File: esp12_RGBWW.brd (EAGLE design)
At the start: 51.1 x 34.9 mm, 35 parts, among them Q1 AOD2910SMD, Q2 AOD2910SMD, Q3 AOD2910SMD, Q4 AOD2910SMD, Q5 AOD2910SMD, U1 TPS5410DR

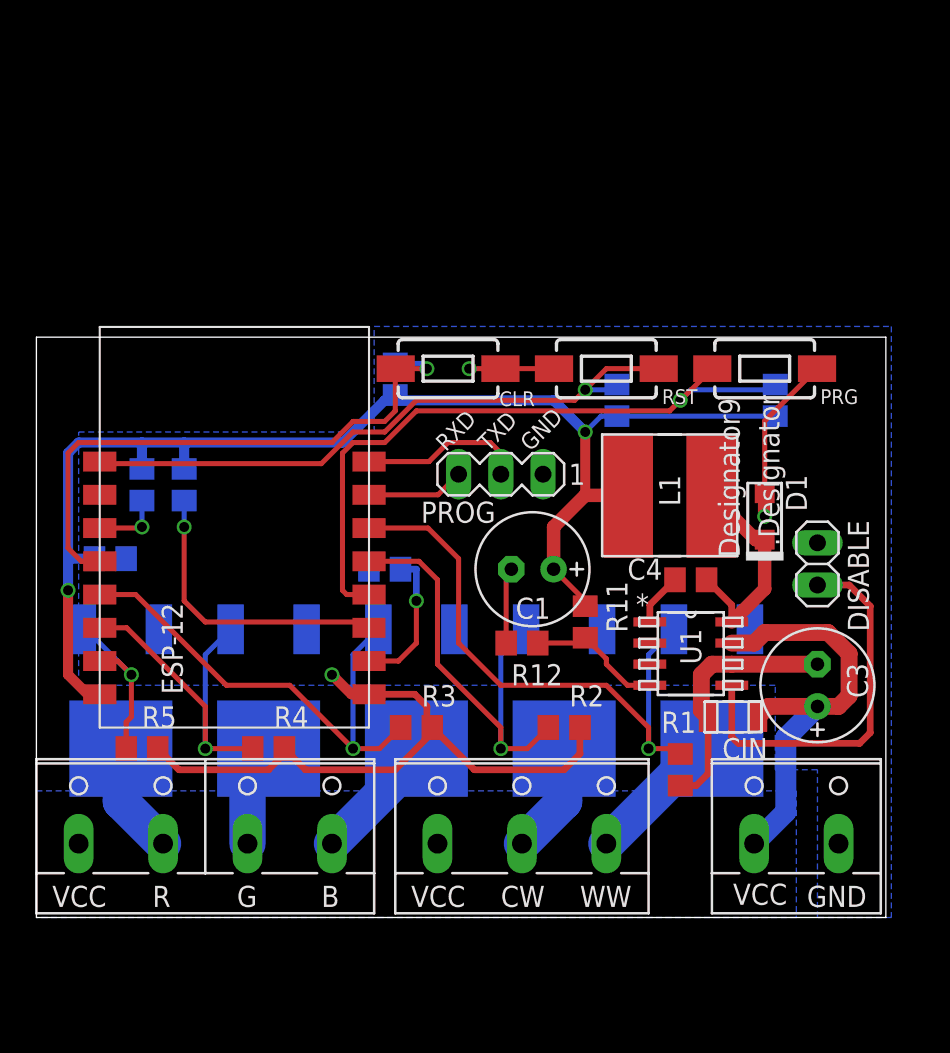
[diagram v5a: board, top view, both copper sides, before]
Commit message: some power supply improvements
added a snubber network to PH (140MHz) plus a 10nF cap on the +3V3 line
Added low impedance floodfills for +3V3 and PH where applicable
switched the location of the RST and PRG switches since it seems easier to have the RST on the outside
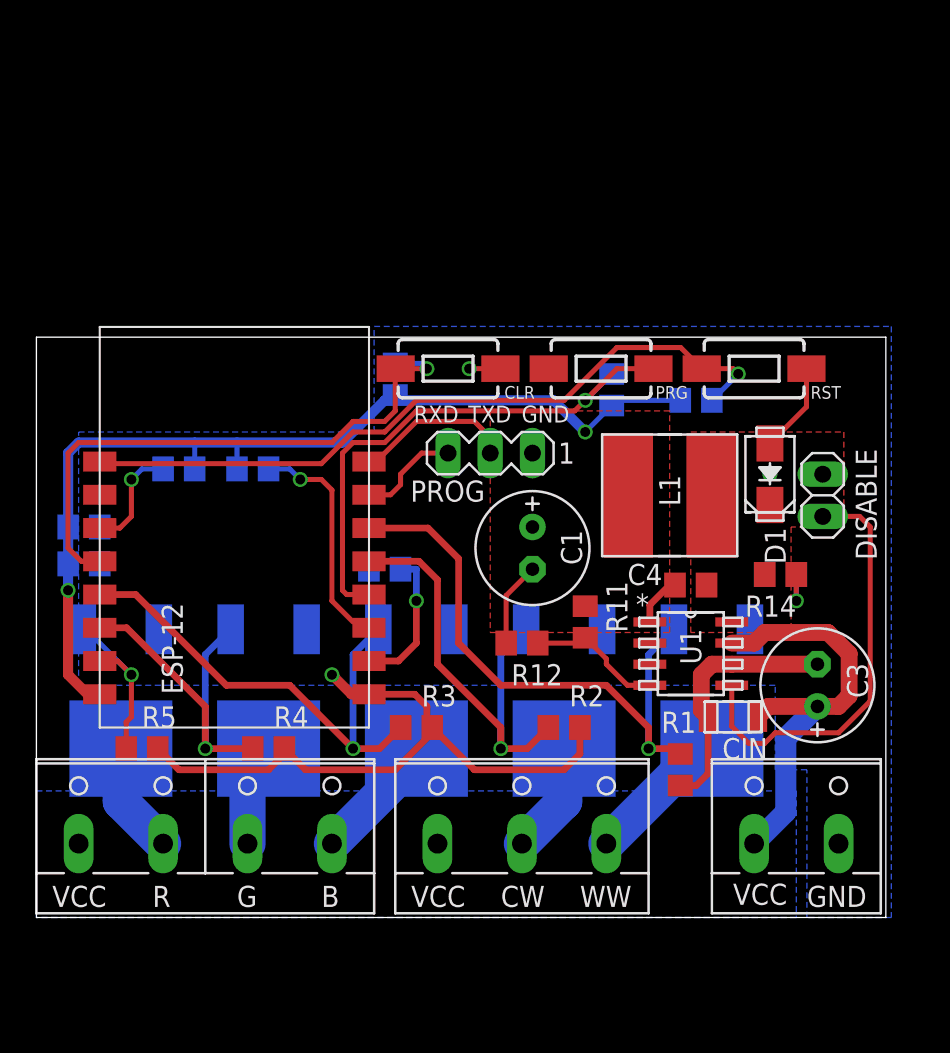
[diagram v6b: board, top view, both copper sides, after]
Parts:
- added C5: 10n, rcl:C0805
- added C6: 1.5p, rcl:C0805
- added R14: 1k, rcl:R0805
- D1: device AcceleratedDesigns_Lib:SOD-123F -> TI_Accelerated_Design_neu:SMA
- moved R13 9.86 mm to (33.3, 31.8)
- moved PRG 9.84 mm to (32.7, 33.0), turned to 180 degrees
- moved RST 8.89 mm to (41.9, 33.0), turned to 180 degrees
- moved R10 4.76 mm to (38.4, 31.1), turned to 180 degrees
- moved R7 4.24 mm to (11.7, 27.0), turned to 0 degrees
- moved DISABLE 4.14 mm to (46.0, 25.4), turned to 90 degrees
- moved D1 2.56 mm to (42.9, 26.7)
- moved C2 2.48 mm to (1.59, 23.5)
- moved R9 2.42 mm to (7.30, 27.0), turned to 180 degrees
- moved PROG 1.42 mm to (26.0, 27.9)
- moved C1 1.27 mm to (28.6, 22.2), turned to 270 degrees
- moved C4 0.32 mm to (38.1, 20.0)
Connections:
- new net SNUB: C6.1, R14.1
- net +3V3: now also C5.2
- net ENA: now also DISABLE.1; no longer DISABLE.2
- net GND: now also C5.1, C6.2, DISABLE.2; no longer DISABLE.1
- net PH: now also R14.2
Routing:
- net +3V3: track 83.9 -> 60.1 mm
- net PH: track 15.7 -> 3.40 mm
- net GND: track 76.0 -> 68.5 mm
- net PRG_S: track 40.4 -> 33.0 mm
- net RST_S: track 38.1 -> 44.3 mm
- net G2: track 17.8 -> 13.9 mm
- net SNUB: track 0.00 -> 3.18 mm, vias 0 -> 1
- net ENA: track 23.2 -> 25.9 mm
- net CH_PD: track 4.16 -> 6.59 mm
- added copper zone on layer 1, net +3V3
- added copper zone on layer 1, net PH

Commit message: more board improvements
- floodfills for VCC, PH and top layer +3V3 nods
- RC snubber for PH node
- additional 10nF cap close to the ESPs 3.3V
- cleaned up the GND layer a bit
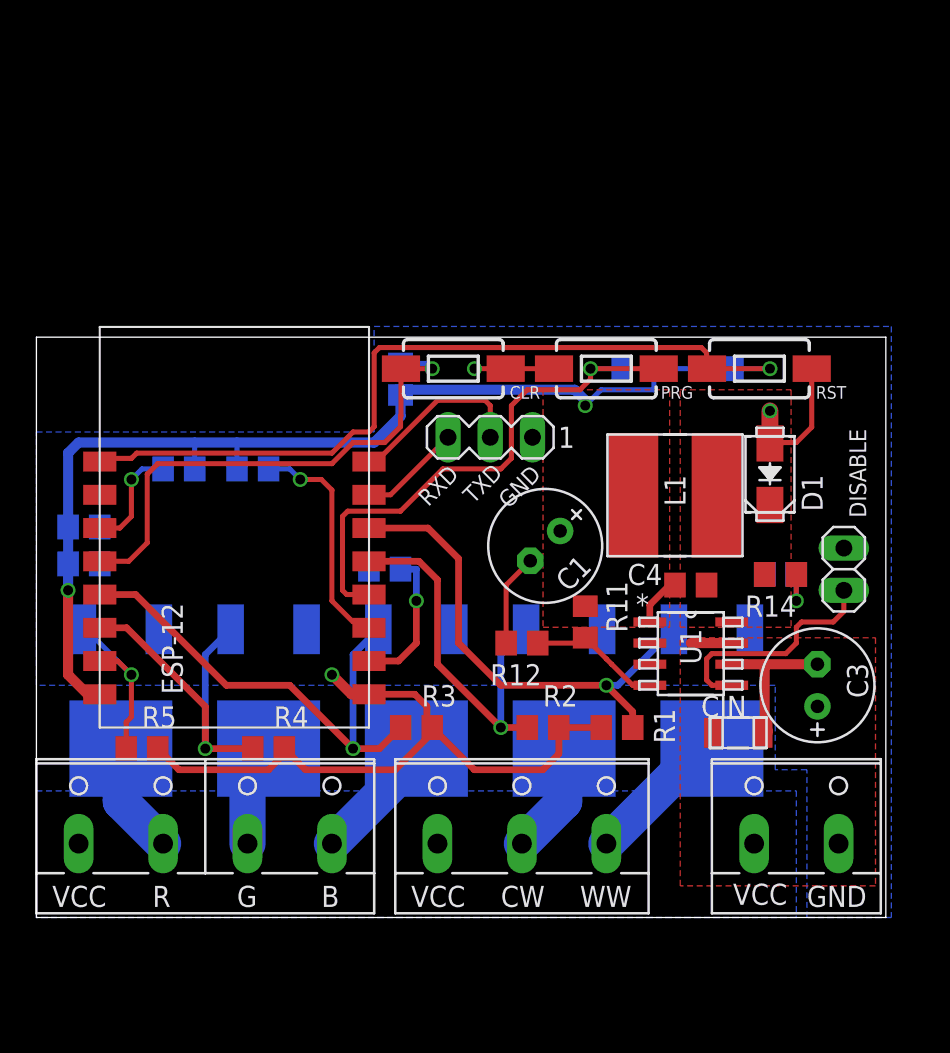
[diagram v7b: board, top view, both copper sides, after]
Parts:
- moved DISABLE 4.62 mm to (47.3, 21.0)
- moved R1 4.58 mm to (33.7, 11.4), turned to 0 degrees
- moved R10 2.29 mm to (39.7, 33.0)
- moved R13 2.03 mm to (34.9, 33.0), turned to 180 degrees
- moved R2 1.27 mm to (29.2, 11.4)
- moved CIN 1.00 mm to (41.0, 11.1), turned to 180 degrees
- moved PROG 0.95 mm to (26.0, 28.9)
- moved C1 0.78 mm to (29.3, 22.4), turned to 225 degrees
- moved L1 0.32 mm to (37.1, 25.4)
- moved PRG 0.32 mm to (33.0, 33.0)
- moved RST 0.32 mm to (42.2, 33.0)
- moved CLR 0.32 mm to (23.8, 33.0)
- moved R8 0.32 mm to (20.6, 32.4)
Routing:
- net +12V: track 26.2 -> 2.46 mm
- net ENA: track 25.9 -> 14.2 mm
- net RGB-WW: track 35.9 -> 29.8 mm
- net RST_S: track 44.3 -> 49.2 mm
- net RGB-CW: track 27.5 -> 23.2 mm
- net CLR_S: track 35.4 -> 31.5 mm
- net PH: track 3.40 -> 0.00 mm
- net +3V3: track 60.1 -> 62.5 mm
- net GND: track 68.5 -> 70.1 mm
- net TXD: track 9.64 -> 10.9 mm
- added copper zone on layer 1, net +12V

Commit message: yet more minor changes on the input side
removed the snubber pads
created a lower impedance GND path
swiched RXD and TXD for some more elegant routing and better fit with the usual USB/UART connectors (straight cable now switches RX/TX)
minor silkscreen corrections for better legibility
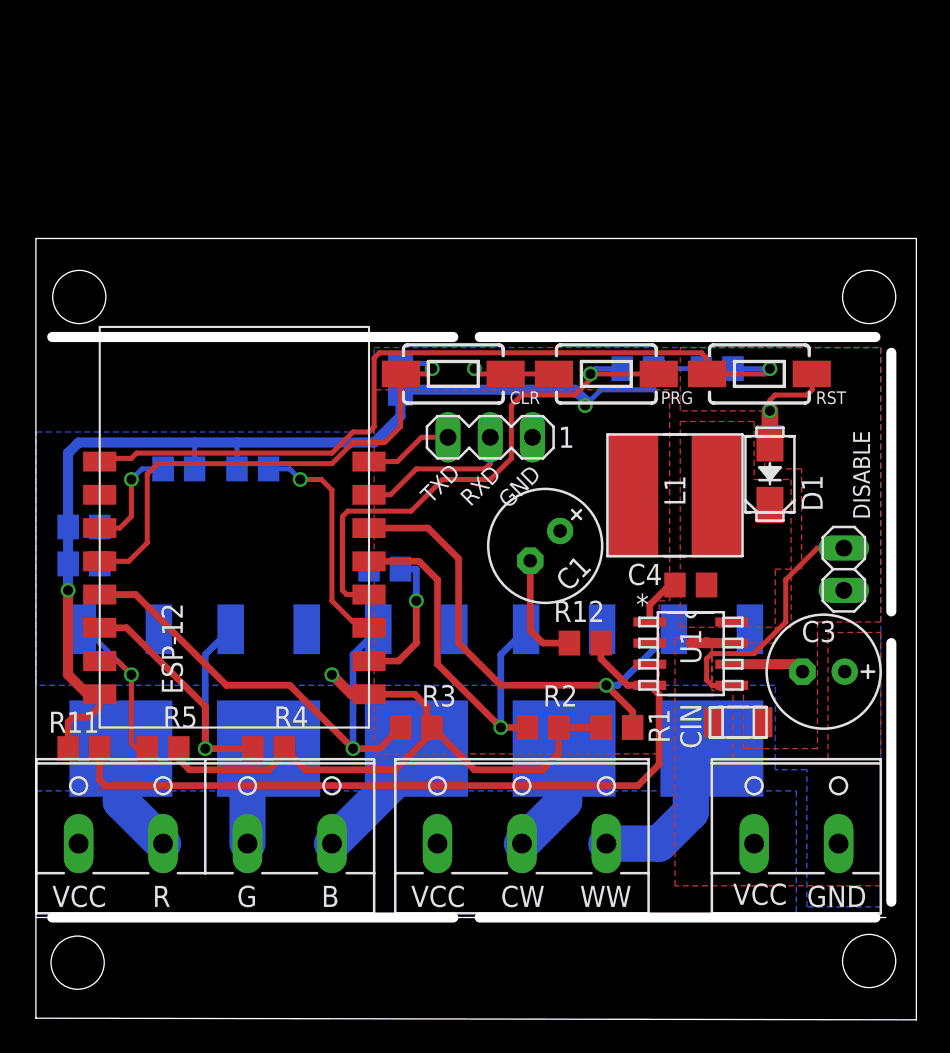
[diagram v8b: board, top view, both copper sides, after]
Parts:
- removed C6: 1.5p, rcl:C0805
- removed R14: 1k, rcl:R0805
- C1: value (none) -> 440nF
- moved R11 31.1 mm to (1.59, 10.2), turned to 180 degrees
- moved R12 3.81 mm to (31.8, 16.5)
- moved R5 1.27 mm to (6.35, 10.2)
- moved C3 0.90 mm to (46.1, 14.8), turned to 180 degrees
- moved CIN 0.63 mm to (41.0, 11.7)
- moved CLR 0.32 mm to (23.8, 32.7)
- moved PRG 0.32 mm to (33.0, 32.7)
- moved RST 0.32 mm to (42.2, 32.7)
- turned DISABLE to 270 degrees
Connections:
- removed net SNUB: C6.1, R14.1
- net GND: no longer C6.2
- net PH: no longer R14.2
- net RXD: now also PROG.2; no longer PROG.3
- net TXD: now also PROG.3; no longer PROG.2
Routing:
- net SENS: track 8.51 -> 45.8 mm
- net TXD: track 10.9 -> 5.36 mm
- net GND: track 70.1 -> 65.0 mm
- net +3V3: track 62.5 -> 66.8 mm
- net RXD: track 6.19 -> 9.66 mm
- net SNUB: track 3.18 -> 0.00 mm, vias 1 -> 0
- net ENA: track 14.2 -> 15.4 mm
- net WW: track 8.98 -> 10.2 mm
- added copper zone on layer 1, net GND
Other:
- board size 51.1 x 34.9 mm -> 53 x 47 mm
